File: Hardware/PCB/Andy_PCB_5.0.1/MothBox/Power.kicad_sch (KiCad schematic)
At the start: 31 parts, among them J1 DB141V-2.54-4P, J2 DB141V-2.54-4P, J3 DB141V-2.54-4P, Q1 JMTV210P02A, Q2 AO3400A, Q8 JMTV210P02A, U1 Place Holder voltage regulator, U2 XL4015E1, U3 INA219BIDCNT

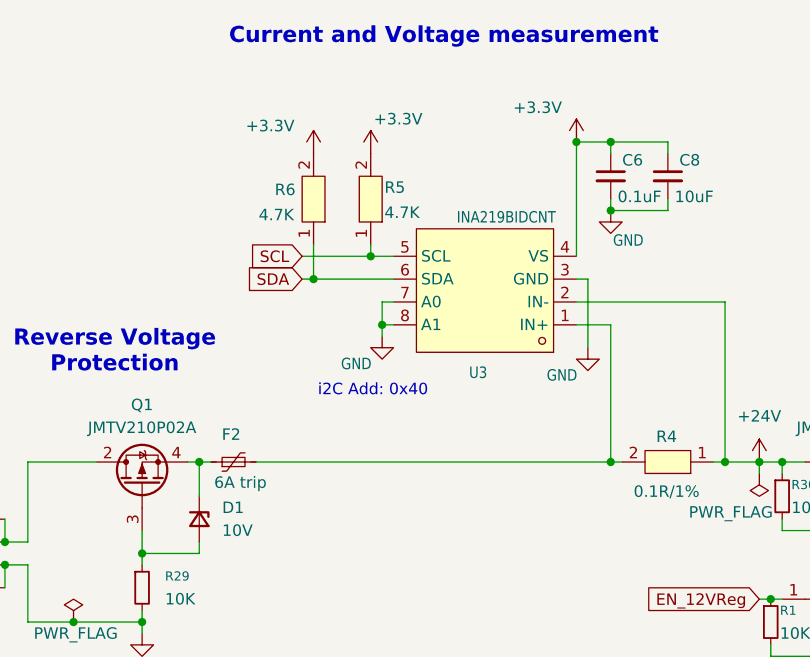
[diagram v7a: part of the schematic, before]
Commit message: updated MothBeam PCB Edge and MothBox PCB
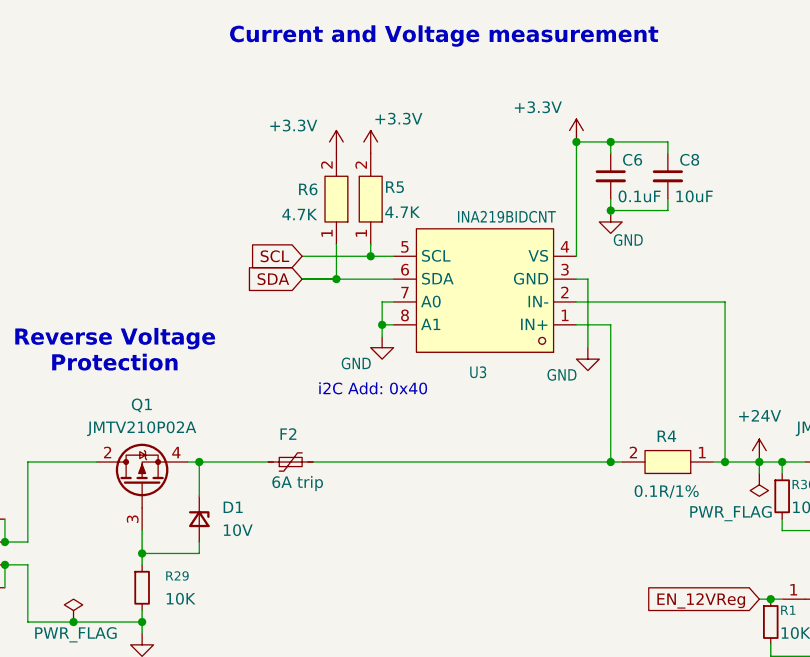
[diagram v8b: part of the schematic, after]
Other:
- moved on the sheet: F2, R6
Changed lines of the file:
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@@
 	)
 	(junction
-		(at 104.14 52.07)
+		(at 100.33 54.61)
 		(diameter 0)
 		(color 0 0 0 0)
 	)
 	(junction
-		(at 106.68 138.43)
+		(at 104.14 52.07)
 		(diameter 0)
 		(color 0 0 0 0)
 	)
 	(junction
-		(at 78.74 85.09)
+		(at 106.68 138.43)
 		(diameter 0)
 		(color 0 0 0 0)
 	)
 	(junction
-		(at 97.79 54.61)
+		(at 78.74 85.09)
 		(diameter 0)
 		(color 0 0 0 0)
@@
 	(wire
 		(pts
-			(xy 91.44 74.93) (xy 130.81 74.93)
+			(xy 97.79 74.93) (xy 130.81 74.93)
 		)
 		(stroke
@@
 	(wire
 		(pts
-			(xy 106.68 54.61) (xy 97.79 54.61)
+			(xy 106.68 54.61) (xy 100.33 54.61)
 		)
 		(stroke
@@
 	(wire
 		(pts
-			(xy 85.09 74.93) (xy 86.36 74.93)
+			(xy 85.09 74.93) (xy 92.71 74.93)
 		)
 		(stroke
@@
 	(wire
 		(pts
+			(xy 96.52 54.61) (xy 100.33 54.61)
+		)
+		(stroke
+			(width 0)
+			(type default)
+		)
+	)
+	(wire
+		(pts
 			(xy 66.04 74.93) (xy 66.04 83.82)
 		)
@@
 	(wire
 		(pts
-			(xy 97.79 54.61) (xy 96.52 54.61)
+			(xy 96.52 54.61) (xy 100.33 54.61)
 		)
 		(stroke
@@
 	(wire
 		(pts
-			(xy 97.79 50.8) (xy 97.79 54.61)
+			(xy 100.33 50.8) (xy 100.33 54.61)
 		)
 		(stroke
@@
 	(symbol
 		(lib_id "MothBox_Symbol_Library:Polyfuse_Small")
-		(at 88.9 74.93 90)
+		(at 95.25 74.93 90)
 		(unit 1)
 		(exclude_from_sim no)
@@
 		(dnp no)
 		(property "Reference" "F2"
-			(at 88.646 71.882 90)
+			(at 94.996 71.882 90)
 			(effects
 				(font
@@
 		)
 		(property "Value" "6A trip"
-			(at 89.662 77.216 90)
+			(at 96.012 77.216 90)
 			(effects
 				(font
@@
 		)
 		(property "Footprint" "Fuse:Fuse_1812_4532Metric"
-			(at 93.98 73.66 0)
+			(at 100.33 73.66 0)
 			(effects
 				(font
@@
 		)
 		(property "Datasheet" "~"
-			(at 88.9 74.93 0)
+			(at 95.25 74.93 0)
 			(effects
 				(font
@@
 		)
 		(property "Description" "Resettable fuse, polymeric positive temperature coefficient, small symbol"
-			(at 88.9 74.93 0)
+			(at 95.25 74.93 0)
 			(effects
 				(font
@@
 		)
 		(property "LCSC" "C7500481"
-			(at 88.9 74.93 90)
+			(at 95.25 74.93 90)
 			(effects
 				(font
@@
 		)
 		(property "AVAILABILITY" ""
-			(at 88.9 74.93 90)
+			(at 95.25 74.93 90)
 			(effects
 				(font
@@
 		)
 		(property "DESCRIPTION" ""
-			(at 88.9 74.93 90)
+			(at 95.25 74.93 90)
 			(effects
 				(font
@@
 		)
 		(property "Link" ""
-			(at 88.9 74.93 90)
+			(at 95.25 74.93 90)
 			(effects
 				(font
@@
 		)
 		(property "PACKAGE" ""
-			(at 88.9 74.93 90)
+			(at 95.25 74.93 90)
 			(effects
 				(font
@@
 		)
 		(property "PRICE" ""
-			(at 88.9 74.93 90)
+			(at 95.25 74.93 90)
 			(effects
 				(font
@@
 		)
 		(property "Ali_Express_Link" ""
-			(at 88.9 74.93 90)
+			(at 95.25 74.93 90)
 			(effects
 				(font
@@
 		)
 		(property "LCSC_PN" ""
-			(at 88.9 74.93 90)
+			(at 95.25 74.93 90)
 			(effects
 				(font
@@
 	(symbol
 		(lib_id "MothBox_Symbol_Library:FRC0603J103TS")
-		(at 97.79 45.72 270)
+		(at 100.33 45.72 270)
 		(mirror x)
 		(unit 1)
@@
 		(dnp no)
 		(property "Reference" "R6"
-			(at 93.472 43.942 90)
+			(at 96.012 43.942 90)
 			(effects
 				(font
@@
 		)
 		(property "Value" "4.7K"
-			(at 91.694 46.736 90)
+			(at 94.234 46.736 90)
 			(effects
 				(font
@@
 		)
 		(property "Footprint" "MothBox_footprints_Library:R_0603_1608Metric"
-			(at 90.17 45.72 0)
+			(at 92.71 45.72 0)
 			(effects
 				(font
@@
 		)
 		(property "Datasheet" ""
-			(at 97.79 45.72 0)
+			(at 100.33 45.72 0)
 			(effects
 				(font
@@
 		)
 		(property "Description" ""
-			(at 97.79 45.72 0)
+			(at 100.33 45.72 0)
 			(effects
 				(font
@@
 		)
 		(property "AVAILABILITY" ""
-			(at 97.79 45.72 90)
+			(at 100.33 45.72 90)
 			(effects
 				(font
@@
 		)
 		(property "DESCRIPTION" ""
-			(at 97.79 45.72 90)
+			(at 100.33 45.72 90)
 			(effects
 				(font
@@
 		)
 		(property "Link" ""
-			(at 97.79 45.72 90)
+			(at 100.33 45.72 90)
 			(effects
 				(font
@@
 		)
 		(property "PACKAGE" ""
-			(at 97.79 45.72 90)
+			(at 100.33 45.72 90)
 			(effects
 				(font
@@
 		)
 		(property "PRICE" ""
-			(at 97.79 45.72 90)
+			(at 100.33 45.72 90)
 			(effects
 				(font
@@
 		)
 		(property "LCSC_Part" "C2930027"
-			(at 97.79 45.72 90)
+			(at 100.33 45.72 90)
 			(effects
 				(font
@@
 		)
 		(property "Ali_Express_Link" ""
-			(at 97.79 45.72 90)
+			(at 100.33 45.72 90)
 			(effects
 				(font
@@
 		)
 		(property "LCSC_PN" ""
-			(at 97.79 45.72 90)
+			(at 100.33 45.72 90)
 			(effects
 				(font
@@
 	(symbol
 		(lib_id "MothBox_Symbol_Library:+3.3V")
-		(at 97.79 40.64 0)
+		(at 100.33 40.64 0)
 		(mirror y)
 		(unit 1)
@@
 		(dnp no)
 		(property "Reference" "#PWR016"
-			(at 97.79 44.45 0)
+			(at 100.33 44.45 0)
 			(effects
 				(font
@@
 		)
 		(property "Value" "+3.3V"
-			(at 92.964 37.592 0)
+			(at 95.504 37.592 0)
 			(effects
 				(font
@@
 		)
 		(property "Footprint" ""
-			(at 97.79 40.64 0)
+			(at 100.33 40.64 0)
 			(effects
 				(font
@@
 		)
 		(property "Datasheet" ""
-			(at 97.79 40.64 0)
+			(at 100.33 40.64 0)
 			(effects
 				(font
@@
 		)
 		(property "Description" "Power symbol creates a global label with name \"+3.3V\""
-			(at 97.79 40.64 0)
+			(at 100.33 40.64 0)
 			(effects
 				(font
